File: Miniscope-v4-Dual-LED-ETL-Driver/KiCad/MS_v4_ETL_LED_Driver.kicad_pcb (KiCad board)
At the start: 6 copper layers, 9.7 x 10.5 mm, 32 parts, among them J1 Conn_01x01, J10 Conn_01x05, J6 Conn_01x01, J7 Conn_01x01, U1 MAX14574EWL+, U2 TPL0102-100RUCR, U3 LTC3218, U4 LTC3218

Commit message: Mini update: switched layers
Moved layer 3 (3V3) to layer 2. GND on Layer 5
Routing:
- added copper zone on In1.Cu, net +3V3
- removed copper zone on In3.Cu, net +3V3
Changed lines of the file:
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@@
     (1 In1.Cu signal)
     (2 In2.Cu signal)
-    (3 In3.Cu power hide)
+    (3 In3.Cu power)
     (4 In4.Cu power)
     (31 B.Cu signal)
@@
   (segment (start 15.1718 16.1562) (end 14.607674 15.592074) (width 0.2032) (layer F.Cu) (net 13))
   (segment (start 15.51 16.1562) (end 15.1718 16.1562) (width 0.2032) (layer F.Cu) (net 13))
-  (segment (start 14.607674 14.476284) (end 14.607674 14.794482) (width 0.2032) (layer In1.Cu) (net 13))
+  (segment (start 14.607674 14.476284) (end 14.607674 14.794482) (width 0.2032) (layer In3.Cu) (net 13))
   (segment (start 14.607674 15.11268) (end 14.607674 14.794482) (width 0.2032) (layer F.Cu) (net 13))
-  (segment (start 14.607674 14.002326) (end 14.607674 14.476284) (width 0.2032) (layer In1.Cu) (net 13))
-  (segment (start 14.9 13.71) (end 14.607674 14.002326) (width 0.2032) (layer In1.Cu) (net 13))
+  (segment (start 14.607674 14.002326) (end 14.607674 14.476284) (width 0.2032) (layer In3.Cu) (net 13))
+  (segment (start 14.9 13.71) (end 14.607674 14.002326) (width 0.2032) (layer In3.Cu) (net 13))
   (segment (start 14.607674 15.592074) (end 14.607674 15.11268) (width 0.2032) (layer F.Cu) (net 13))
   (segment (start 14.675001 14.724999) (end 14.607674 14.792326) (width 0.0889) (layer B.Cu) (net 13))
@@
   (segment (start 13.487381 17.9388) (end 13.413486 18.012695) (width 0.2032) (layer F.Cu) (net 15))
   (via (at 13.413486 18.012695) (size 0.45) (drill 0.2) (layers F.Cu B.Cu) (net 15))
-  (segment (start 13.772696 18.012695) (end 14.064201 18.3042) (width 0.152) (layer In1.Cu) (net 15))
-  (segment (start 13.413486 18.012695) (end 13.772696 18.012695) (width 0.152) (layer In1.Cu) (net 15))
+  (segment (start 13.772696 18.012695) (end 14.064201 18.3042) (width 0.152) (layer In3.Cu) (net 15))
+  (segment (start 13.413486 18.012695) (end 13.772696 18.012695) (width 0.152) (layer In3.Cu) (net 15))
   (segment (start 14.8776 17.9388) (end 15.131102 17.9388) (width 0.152) (layer F.Cu) (net 15))
   (via (at 15.5542 18.1742) (size 0.45) (drill 0.2) (layers F.Cu B.Cu) (net 15))
-  (segment (start 14.064201 18.3042) (end 15.2842 18.3042) (width 0.152) (layer In1.Cu) (net 15))
-  (segment (start 15.4142 18.1742) (end 15.5542 18.1742) (width 0.152) (layer In1.Cu) (net 15))
-  (segment (start 15.2842 18.3042) (end 15.4142 18.1742) (width 0.152) (layer In1.Cu) (net 15))
+  (segment (start 14.064201 18.3042) (end 15.2842 18.3042) (width 0.152) (layer In3.Cu) (net 15))
+  (segment (start 15.4142 18.1742) (end 15.5542 18.1742) (width 0.152) (layer In3.Cu) (net 15))
+  (segment (start 15.2842 18.3042) (end 15.4142 18.1742) (width 0.152) (layer In3.Cu) (net 15))
   (segment (start 15.3188 17.9388) (end 15.5542 18.1742) (width 0.152) (layer F.Cu) (net 15))
   (segment (start 14.8776 17.9388) (end 15.3188 17.9388) (width 0.152) (layer F.Cu) (net 15))
@@
   (segment (start 13.9142 20.6442) (end 13.9282 20.6582) (width 0.152) (layer F.Cu) (net 15))
   (via (at 14.04 19.73) (size 0.45) (drill 0.2) (layers F.Cu B.Cu) (net 15))
-  (segment (start 13.413486 18.012695) (end 14.04 18.639209) (width 0.0889) (layer In1.Cu) (net 15))
-  (segment (start 14.04 18.639209) (end 14.04 19.411802) (width 0.0889) (layer In1.Cu) (net 15))
-  (segment (start 14.04 19.411802) (end 14.04 19.73) (width 0.0889) (layer In1.Cu) (net 15))
+  (segment (start 13.413486 18.012695) (end 14.04 18.639209) (width 0.0889) (layer In3.Cu) (net 15))
+  (segment (start 14.04 18.639209) (end 14.04 19.411802) (width 0.0889) (layer In3.Cu) (net 15))
+  (segment (start 14.04 19.411802) (end 14.04 19.73) (width 0.0889) (layer In3.Cu) (net 15))
   (segment (start 14.748 20.6582) (end 14.04 19.9502) (width 0.152) (layer F.Cu) (net 15))
   (segment (start 14.04 19.9502) (end 14.04 19.73) (width 0.152) (layer F.Cu) (net 15))
@@
   (segment (start 20.61426 16.1054) (end 20.61426 16.53426) (width 0.0889) (layer F.Cu) (net 24))
   (segment (start 20.61426 16.53426) (end 20.75 16.67) (width 0.0889) (layer F.Cu) (net 24))
-  (segment (start 20.8 17.22) (end 20.8 17) (width 0.0889) (layer In1.Cu) (net 24))
-  (segment (start 20.54 17.48) (end 20.8 17.22) (width 0.2032) (layer In1.Cu) (net 24))
-  (segment (start 19.950024 17.48) (end 20.54 17.48) (width 0.2032) (layer In1.Cu) (net 24))
-  (segment (start 19.870022 17.560002) (end 19.950024 17.48) (width 0.2032) (layer In1.Cu) (net 24))
-  (segment (start 15.470362 17.560002) (end 19.870022 17.560002) (width 0.2032) (layer In1.Cu) (net 24))
-  (segment (start 12.79652 16.537939) (end 14.448299 16.537939) (width 0.2032) (layer In1.Cu) (net 24))
-  (segment (start 14.448299 16.537939) (end 15.470362 17.560002) (width 0.2032) (layer In1.Cu) (net 24))
+  (segment (start 12.79652 16.537939) (end 14.448299 16.537939) (width 0.2032) (layer In3.Cu) (net 24))
+  (segment (start 14.448299 16.537939) (end 15.470362 17.560002) (width 0.2032) (layer In3.Cu) (net 24))
+  (segment (start 20.8 17.22) (end 20.8 17) (width 0.0889) (layer In3.Cu) (net 24))
+  (segment (start 19.870022 17.560002) (end 19.950024 17.48) (width 0.2032) (layer In3.Cu) (net 24))
+  (segment (start 15.470362 17.560002) (end 19.870022 17.560002) (width 0.2032) (layer In3.Cu) (net 24))
+  (segment (start 20.54 17.48) (end 20.8 17.22) (width 0.2032) (layer In3.Cu) (net 24))
+  (segment (start 19.950024 17.48) (end 20.54 17.48) (width 0.2032) (layer In3.Cu) (net 24))
   (via (at 13.413486 17.047496) (size 0.45) (drill 0.2) (layers F.Cu B.Cu) (net 25))
   (segment (start 13.413486 17.047496) (end 13.760982 16.7) (width 0.152) (layer In2.Cu) (net 25))
@@
   (segment (start 17.12 13.72) (end 16.579998 13.72) (width 0.2032) (layer F.Cu) (net 29))
   (via (at 16.62 17.09) (size 0.45) (drill 0.2) (layers F.Cu B.Cu) (net 29))
-  (segment (start 16.579998 13.72) (end 16.579998 17.049998) (width 0.152) (layer In1.Cu) (net 29))
+  (segment (start 16.579998 13.72) (end 16.579998 17.049998) (width 0.152) (layer In3.Cu) (net 29))
   (segment (start 15.9226 17.2988) (end 16.1314 17.09) (width 0.254) (layer F.Cu) (net 29))
   (segment (start 15.9226 17.4938) (end 15.9226 17.2988) (width 0.0889) (layer F.Cu) (net 29))
-  (segment (start 16.579998 17.049998) (end 16.62 17.09) (width 0.152) (layer In1.Cu) (net 29))
+  (segment (start 16.579998 17.049998) (end 16.62 17.09) (width 0.152) (layer In3.Cu) (net 29))
   (segment (start 16.301802 17.09) (end 16.62 17.09) (width 0.254) (layer F.Cu) (net 29))
   (segment (start 16.1314 17.09) (end 16.301802 17.09) (width 0.254) (layer F.Cu) (net 29))
@@
     )
   )
-  (zone (net 9) (net_name +3V3) (layer In3.Cu) (hatch edge 0.508)
+  (zone (net 8) (net_name GND) (layer In4.Cu) (hatch edge 0.508)
+    (connect_pads (clearance 0.254))
+    (min_thickness 0.254)
+    (fill yes (arc_segments 32) (thermal_gap 0.508) (thermal_bridge_width 0.508))
+    (polygon
+      (pts
+        (xy 12.5 18.2) (xy 13.17 18.2) (xy 13.17 18.82) (xy 12.49 18.82)
+      )
+    )
+  )
+  (zone (net 9) (net_name +3V3) (layer In1.Cu) (hatch edge 0.508)
+    (connect_pads (clearance 0.254))
+    (min_thickness 0.254)
+    (fill yes (arc_segments 32) (thermal_gap 0.508) (thermal_bridge_width 0.508))
+    (polygon
+      (pts
+        (xy 13.05 18.66) (xy 13.7 18.66) (xy 13.7 19.34) (xy 13.04 19.34)
+      )
+    )
+  )
+  (zone (net 9) (net_name +3V3) (layer In1.Cu) (hatch edge 0.508)
     (connect_pads (clearance 0.254))
     (min_thickness 0.254)
@@
       )
     )
-  )
-  (zone (net 9) (net_name +3V3) (layer In3.Cu) (hatch edge 0.508)
-    (connect_pads (clearance 0.254))
-    (min_thickness 0.254)
-    (fill yes (arc_segments 32) (thermal_gap 0.508) (thermal_bridge_width 0.508))
-    (polygon
-      (pts
-        (xy 13.05 18.66) (xy 13.7 18.66) (xy 13.7 19.34) (xy 13.04 19.34)
-      )
-    )
-  )
-  (zone (net 8) (net_name GND) (layer In4.Cu) (hatch edge 0.508)
-    (connect_pads (clearance 0.254))
-    (min_thickness 0.254)
-    (fill yes (arc_segments 32) (thermal_gap 0.508) (thermal_bridge_width 0.508))
-    (polygon
-      (pts
-        (xy 12.5 18.2) (xy 13.17 18.2) (xy 13.17 18.82) (xy 12.49 18.82)
-      )
-    )

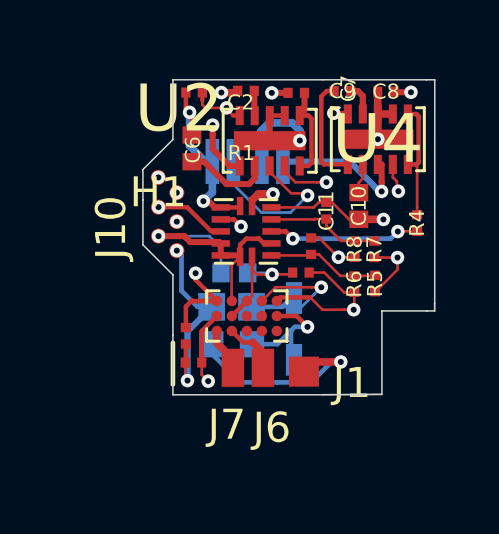
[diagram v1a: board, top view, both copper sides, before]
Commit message: Final version
Fixed:

* Flipped LEDs
* Ground plane
* Added extra silk to "1" pads636

To do

* Final check
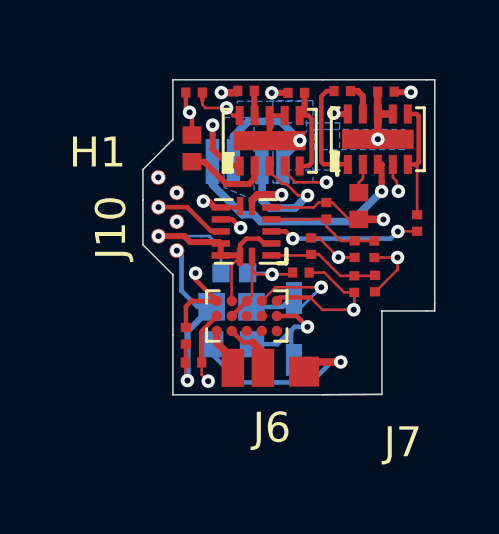
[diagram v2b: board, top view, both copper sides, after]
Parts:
- moved D2 1.65 mm to (16.6, 16.0), turned to 0 degrees
- moved D3 1.65 mm to (14.9, 16.0), turned to 0 degrees
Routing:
- net Net-(D3-PadA): track 4.67 -> 8.34 mm
- net GND: track 43.8 -> 41.3 mm
- added copper zone on In4.Cu, net +3V3
- added copper zone on B.Cu, net GND
- added copper zone on In1.Cu, net GND
- removed copper zone on In1.Cu, net +3V3
- removed copper zone on In4.Cu, net GND
